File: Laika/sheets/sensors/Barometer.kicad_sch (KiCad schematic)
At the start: 0 parts

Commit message: Created schematic for BMP390L Barometer
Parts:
- added C19, C20: 100n, symbol Device:C
- added U8: BMP390L, BMP390:XDCR_BMP390L, symbol BMP390L:BMP390L
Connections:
- new net +3V3: C19.1, C20.1, U8.1 (VDDIO), U8.10 (VDD)
- new net BARO_CS: U8.6 (~{CS})
- new net BARO_INT: U8.7 (INT/DNC)
- new net BARO_SCLK: U8.2 (SCK/SCL)
- new net BARO_SDI: U8.4 (SDI/SDO/SDA)
- new net BARO_SDO: U8.5 (SDO/DNC/SA0)
- new net GND: C19.2, C20.2, U8.3 (VSS/GND), U8.8 (VSS/GND), U8.9 (VSS/GND)
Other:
- note added: "Barometer"

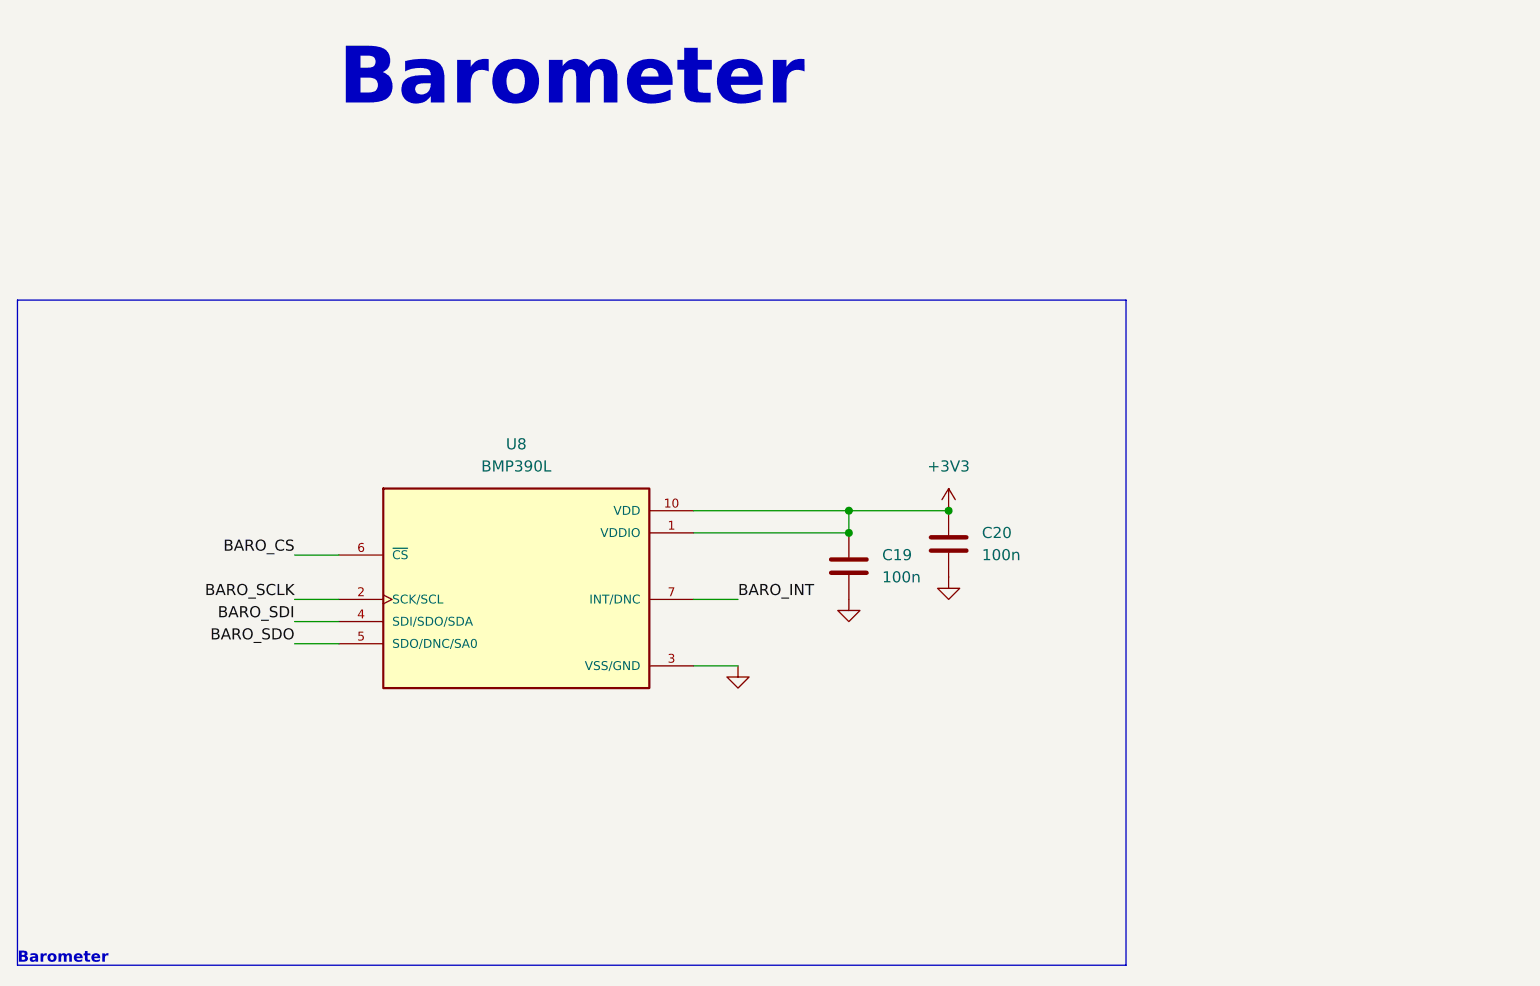
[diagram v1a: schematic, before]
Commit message: Connected sensors to SPI3
Connected Sensor Bus to SPI3. Rearranged GPS reset, pps, and buzzer pins
to other 3.3V logic pins. Connected SPI chip selects. Deleted interrupt
bus from sensors due to lack of 3.3V pins.
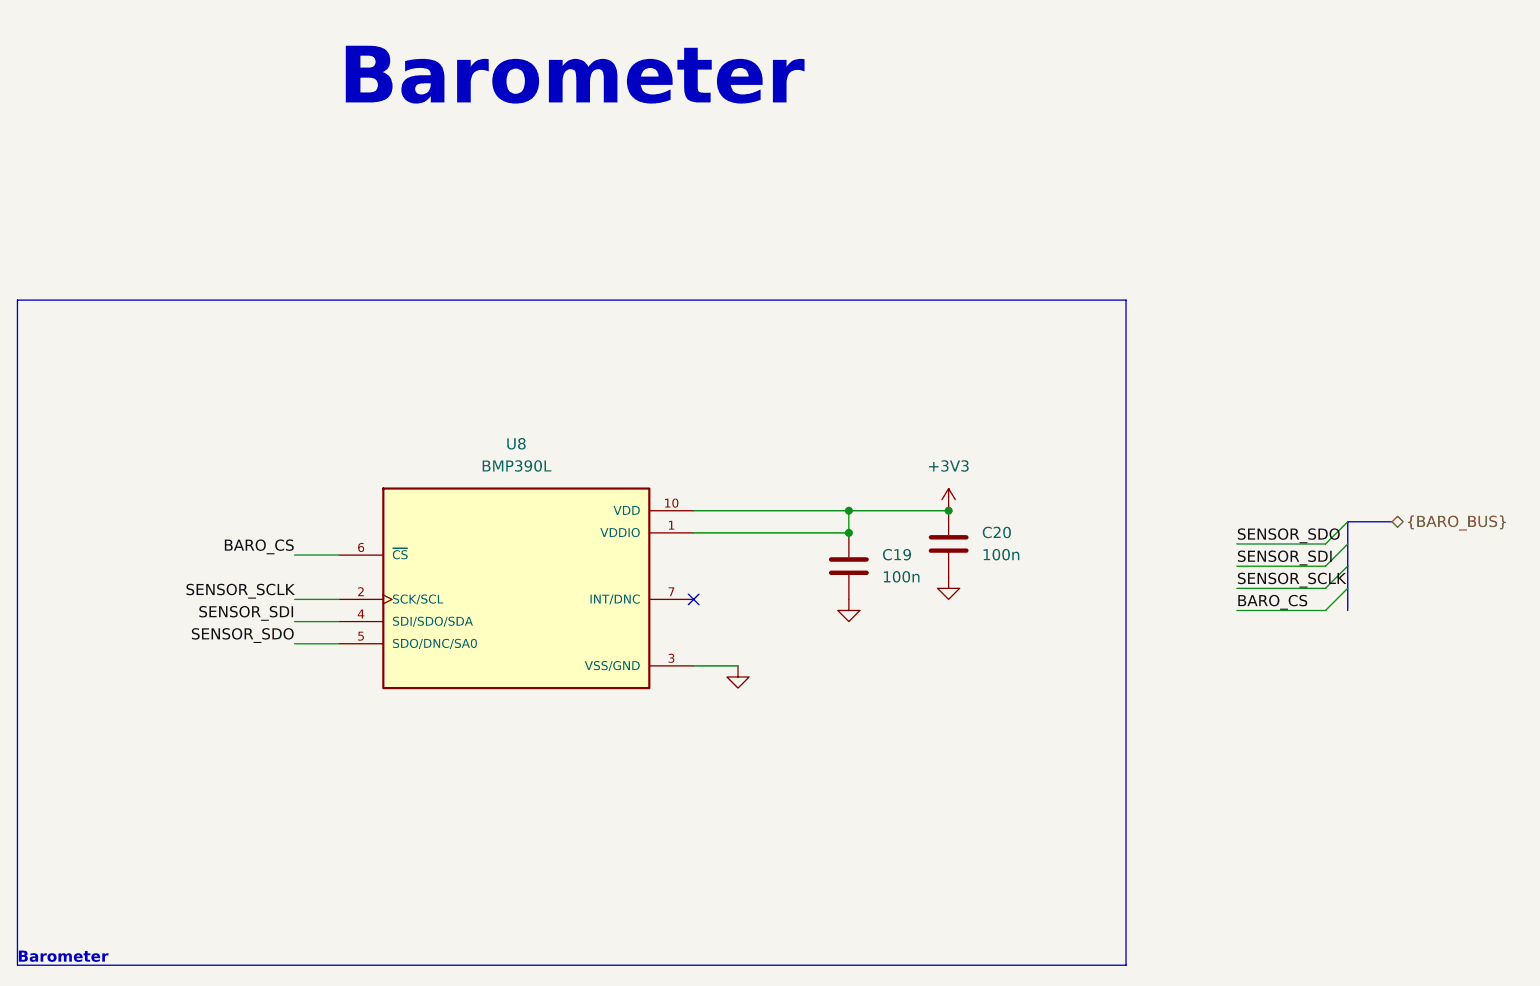
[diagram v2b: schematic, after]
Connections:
- net BARO_INT: no longer names the net of U8.7 (INT/DNC)
- net BARO_SCLK renamed SENSOR_SCLK
- net BARO_SDI renamed SENSOR_SDI
- net BARO_SDO renamed SENSOR_SDO
- no-connect marks 0 -> 1
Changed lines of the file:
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@@
 		(comment 1 "${VARIANT}")
+	)
+	(bus_alias "BARO_BUS"
+		(members "SENSOR_SDO" "SENSOR_SDI" "SENSOR_SCLK" "BARO_CS")
 	)
 	(rectangle
@@
 		(color 0 0 0 0)
 	)
+	(no_connect
+		(at 153.67 85.09)
+	)
+	(bus_entry
+		(at 228.6 78.74)
+		(size -2.54 2.54)
+		(stroke
+			(width 0)
+			(type default)
+		)
+	)
+	(bus_entry
+		(at 228.6 81.28)
+		(size -2.54 2.54)
+		(stroke
+			(width 0)
+			(type default)
+		)
+	)
+	(bus_entry
+		(at 228.6 83.82)
+		(size -2.54 2.54)
+		(stroke
+			(width 0)
+			(type default)
+		)
+	)
+	(bus_entry
+		(at 228.6 76.2)
+		(size -2.54 2.54)
+		(stroke
+			(width 0)
+			(type default)
+		)
+	)
 	(wire
 		(pts
@@
 		)
 	)
+	(bus
+		(pts
+			(xy 228.6 83.82) (xy 228.6 86.36)
+		)
+		(stroke
+			(width 0)
+			(type default)
+		)
+	)
 	(wire
 		(pts
@@
 		)
 	)
+	(bus
+		(pts
+			(xy 233.68 76.2) (xy 228.6 76.2)
+		)
+		(stroke
+			(width 0)
+			(type default)
+		)
+	)
 	(wire
 		(pts
@@
 		)
 	)
+	(bus
+		(pts
+			(xy 228.6 78.74) (xy 228.6 81.28)
+		)
+		(stroke
+			(width 0)
+			(type default)
+		)
+	)
+	(bus
+		(pts
+			(xy 228.6 76.2) (xy 228.6 78.74)
+		)
+		(stroke
+			(width 0)
+			(type default)
+		)
+	)
+	(wire
+		(pts
+			(xy 215.9 86.36) (xy 226.06 86.36)
+		)
+		(stroke
+			(width 0)
+			(type default)
+		)
+	)
 	(wire
 		(pts
@@
 	(wire
 		(pts
-			(xy 158.75 85.09) (xy 153.67 85.09)
-		)
-		(stroke
-			(width 0)
-			(type default)
-		)
-	)
-	(wire
-		(pts
 			(xy 171.45 74.93) (xy 171.45 77.47)
 		)
@@
 	(wire
 		(pts
+			(xy 215.9 83.82) (xy 226.06 83.82)
+		)
+		(stroke
+			(width 0)
+			(type default)
+		)
+	)
+	(wire
+		(pts
 			(xy 107.95 80.01) (xy 113.03 80.01)
 		)
@@
 	(wire
 		(pts
+			(xy 215.9 81.28) (xy 226.06 81.28)
+		)
+		(stroke
+			(width 0)
+			(type default)
+		)
+	)
+	(wire
+		(pts
+			(xy 215.9 78.74) (xy 226.06 78.74)
+		)
+		(stroke
+			(width 0)
+			(type default)
+		)
+	)
+	(bus
+		(pts
+			(xy 228.6 81.28) (xy 228.6 83.82)
+		)
+		(stroke
+			(width 0)
+			(type default)
+		)
+	)
+	(wire
+		(pts
 			(xy 153.67 77.47) (xy 171.45 77.47)
 		)
@@
 		)
 	)
-	(label "BARO_INT"
-		(at 158.75 85.09 0)
-		(effects
-			(font
-				(size 1.27 1.27)
-			)
-			(justify left bottom)
-		)
-	)
-	(label "BARO_SCLK"
+	(label "SENSOR_SCLK"
 		(at 107.95 85.09 180)
 		(effects
@@
 			)
 			(justify right bottom)
+		)
+	)
+	(label "BARO_CS"
+		(at 215.9 86.36 0)
+		(effects
+			(font
+				(size 1.27 1.27)
+			)
+			(justify left bottom)
+		)
+	)
+	(label "SENSOR_SCLK"
+		(at 215.9 83.82 0)
+		(effects
+			(font
+				(size 1.27 1.27)
+			)
+			(justify left bottom)
 		)
 	)
@@
 		)
 	)
-	(label "BARO_SDI"
+	(label "SENSOR_SDO"
+		(at 215.9 78.74 0)
+		(effects
+			(font
+				(size 1.27 1.27)
+			)
+			(justify left bottom)
+		)
+	)
+	(label "SENSOR_SDI"
+		(at 215.9 81.28 0)
+		(effects
+			(font
+				(size 1.27 1.27)
+			)
+			(justify left bottom)
+		)
+	)
+	(label "SENSOR_SDI"
 		(at 107.95 87.63 180)
 		(effects
@@
 		)
 	)
-	(label "BARO_SDO"
+	(label "SENSOR_SDO"
 		(at 107.95 90.17 180)
 		(effects
@@
 		)
 	)
+	(hierarchical_label "{BARO_BUS}"
+		(shape bidirectional)
+		(at 233.68 76.2 0)
+		(effects
+			(font
+				(size 1.27 1.27)
+			)
+			(justify left)
+		)
+	)

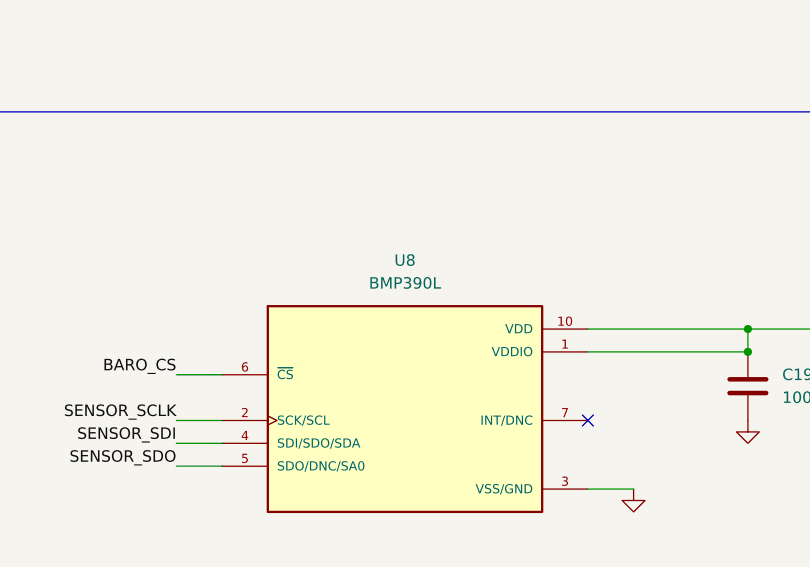
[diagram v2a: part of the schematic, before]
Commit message: Populated BOM with part numbers and footprints
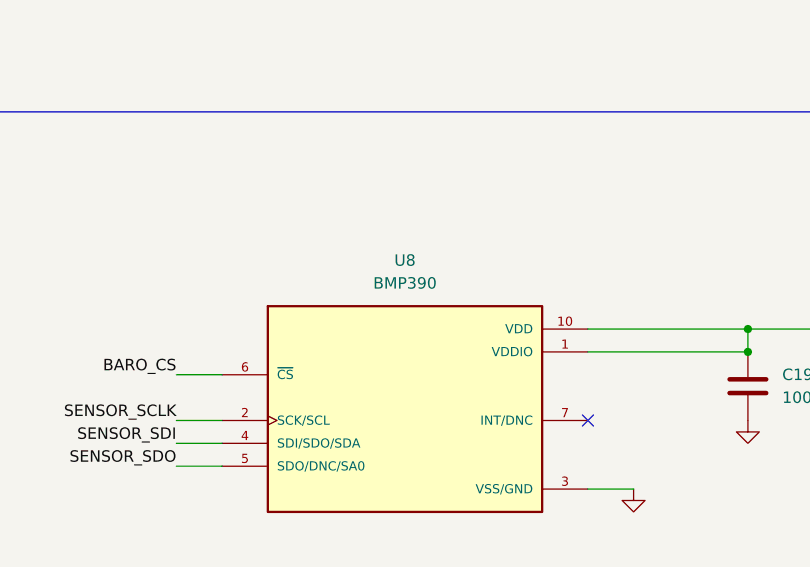
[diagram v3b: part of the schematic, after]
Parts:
- C19, C20: footprint (none) -> Capacitor_SMD:C_0402_1005Metric; JLC Part Type (none) -> Basic; Manafacturer (none) -> Samsung Electro-Mechanics; Part Number (none) -> CL05B104KO5NNNC
- U8: value BMP390L -> BMP390; JLC Part Type (none) -> Extended; Manafacturer (none) -> Bosch Sensortec; Part Number (none) -> BMP390
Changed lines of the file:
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@@
 			)
 		)
-		(property "Footprint" ""
+		(property "Footprint" "Capacitor_SMD:C_0402_1005Metric"
 			(at 172.4152 85.09 0)
 			(effects
@@
 			)
 		)
-		(property "Datasheet" "~"
+		(property "Datasheet" "https://www.samsungsem.com/resources/file/global/support/product_catalog/MLCC.pdf"
 			(at 171.45 81.28 0)
 			(effects
@@
 		)
 		(property "Description" "Unpolarized capacitor"
+			(at 171.45 81.28 0)
+			(effects
+				(font
+					(size 1.27 1.27)
+				)
+				(hide yes)
+			)
+		)
+		(property "JLC Part Type" "Basic"
+			(at 171.45 81.28 0)
+			(effects
+				(font
+					(size 1.27 1.27)
+				)
+				(hide yes)
+			)
+		)
+		(property "Manafacturer" "Samsung Electro-Mechanics"
+			(at 171.45 81.28 0)
+			(effects
+				(font
+					(size 1.27 1.27)
+				)
+				(hide yes)
+			)
+		)
+		(property "Part Number" "CL05B104KO5NNNC"
 			(at 171.45 81.28 0)
 			(effects
@@
 			)
 		)
-		(property "Footprint" ""
+		(property "Footprint" "Capacitor_SMD:C_0402_1005Metric"
 			(at 183.8452 82.55 0)
 			(effects
@@
 			)
 		)
-		(property "Datasheet" "~"
+		(property "Datasheet" "https://www.samsungsem.com/resources/file/global/support/product_catalog/MLCC.pdf"
 			(at 182.88 78.74 0)
 			(effects
@@
 		)
 		(property "Description" "Unpolarized capacitor"
+			(at 182.88 78.74 0)
+			(effects
+				(font
+					(size 1.27 1.27)
+				)
+				(hide yes)
+			)
+		)
+		(property "JLC Part Type" "Basic"
+			(at 182.88 78.74 0)
+			(effects
+				(font
+					(size 1.27 1.27)
+				)
+				(hide yes)
+			)
+		)
+		(property "Manafacturer" "Samsung Electro-Mechanics"
+			(at 182.88 78.74 0)
+			(effects
+				(font
+					(size 1.27 1.27)
+				)
+				(hide yes)
+			)
+		)
+		(property "Part Number" "CL05B104KO5NNNC"
 			(at 182.88 78.74 0)
 			(effects
@@
 			)
 		)
-		(property "Value" "BMP390L"
+		(property "Value" "BMP390"
 			(at 133.35 69.85 0)
 			(effects
@@
 				(hide yes)
 			)
+		)
+		(property "JLC Part Type" "Extended"
+			(at 133.35 85.09 0)
+			(effects
+				(font
+					(size 1.27 1.27)
+				)
+				(hide yes)
+			)
+		)
+		(property "Manafacturer" "Bosch Sensortec"
+			(at 133.35 85.09 0)
+			(effects
+				(font
+					(size 1.27 1.27)
+				)
+				(hide yes)
+			)
+		)
+		(property "Part Number" "BMP390"
+			(at 133.35 85.09 0)
+			(effects
+				(font
+					(size 1.27 1.27)
+				)
+				(hide yes)
+			)
